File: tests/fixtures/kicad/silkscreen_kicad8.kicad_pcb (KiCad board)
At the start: 2 copper layers, 1 part, among them U1 hidden

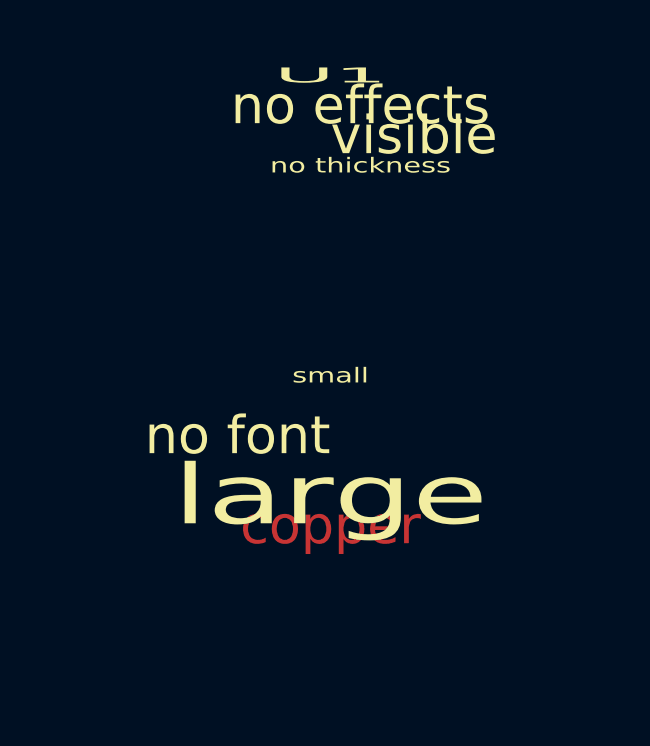
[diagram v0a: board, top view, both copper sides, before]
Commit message: KiCad silkscreen min-text: address review (hide token position, missing-size tests, final-stage diagnostics)
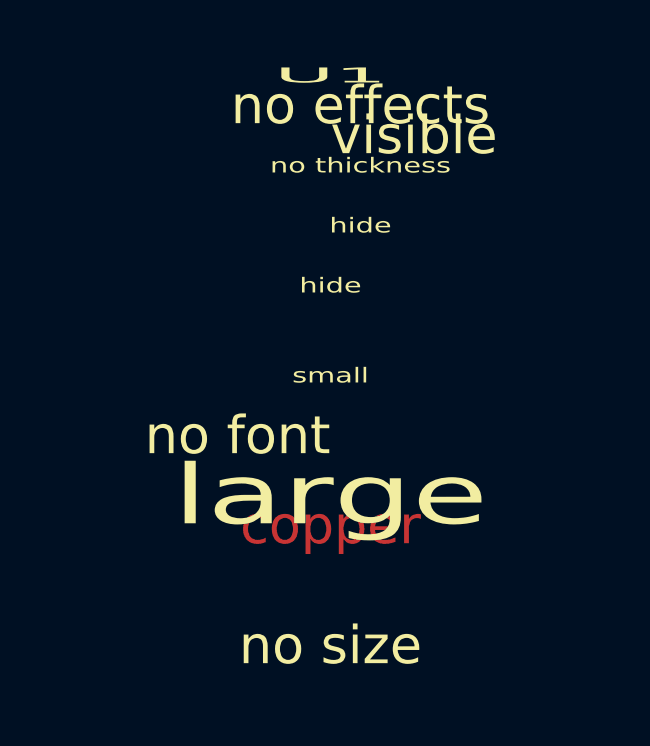
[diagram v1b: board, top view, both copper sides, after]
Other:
- board text added: "hidden bare"
- board text added: "hidden node"
- board text added: "hide"
- board text added: "no dimensions"
- board text added: "no size"
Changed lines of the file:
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@@
       (effects (font (size 0.1 0.1)) hide))
     (property "Shown" "visible" (at 0 6) (layer "B.SilkS") (hide no))
+    (property "VisibleHide" "hide" (at 0 7) (layer "F.SilkS")
+      (effects (font (size 0.5 0.7) (thickness 0.08))))
+    (property "hide" "visible" (at 0 8) (layer "B.SilkS"))
+    (property "HiddenBare" "hidden" (at 0 9) (layer "F.SilkS") hide)
     (fp_text user "small" (at 1 0) (layer "B.SilkS")
       (effects (font (size 2 0.5) (thickness 0.08))))
@@
       (effects (font (size 0.5 0.7))))
     (fp_text value "hidden" (at 1 4) (layer "F.SilkS") hide)
+    (fp_text user "hide" (at 1 5) (layer "F.SilkS")
+      (effects (font (size 0.5 0.7) (thickness 0.08))))
+    (fp_text user "hidden effects" (at 1 6) (layer "B.SilkS")
+      (effects (font (size 0.1 0.1)) (hide yes)))
   )
   (gr_text "small" (at 10 20) (layer "F.SilkS")
@@
     (effects (font (size 2 3) (thickness 0.3))))
   (gr_text "copper" (at 10 25) (layer "F.Cu"))
+  (gr_text "hide" (at 10 26) (layer "B.SilkS")
+    (effects (font (size 0.5 0.7) (thickness 0.08))))
+  (gr_text "hidden bare" (at 10 27) (layer "F.SilkS") hide)
+  (gr_text "hidden node" (at 10 28) (layer "B.SilkS") (hide yes))
+  (gr_text "no size" (at 10 29) (layer "F.SilkS")
+    (effects (font (thickness 0.3))))
+  (gr_text "no dimensions" (at 10 30) (layer "B.SilkS") (effects (font bold)))
 )
